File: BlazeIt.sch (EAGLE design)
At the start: 29 parts, among them IC1 L293D, IC2 L293D, Q1 200mA/40V, Q2 200mA/40V, Q3 200mA/40V, Q4 200mA/40V, U3 V_REG_317SINK

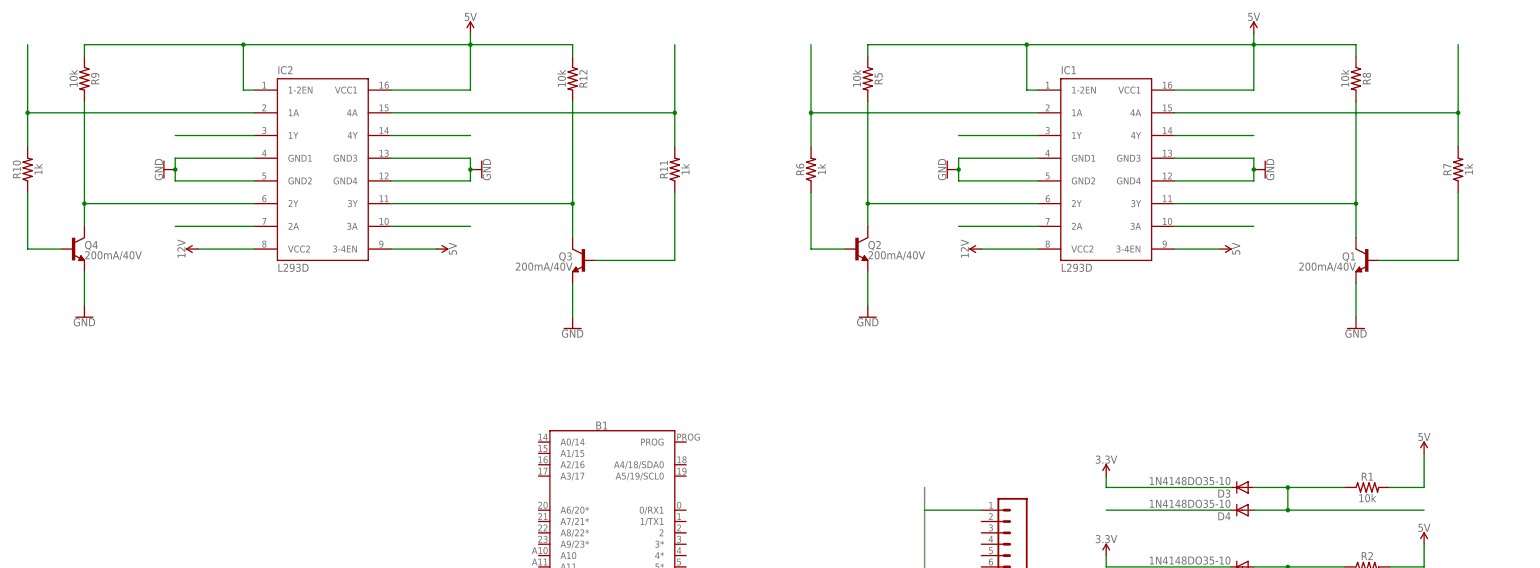
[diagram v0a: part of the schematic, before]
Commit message: added motor control wiring
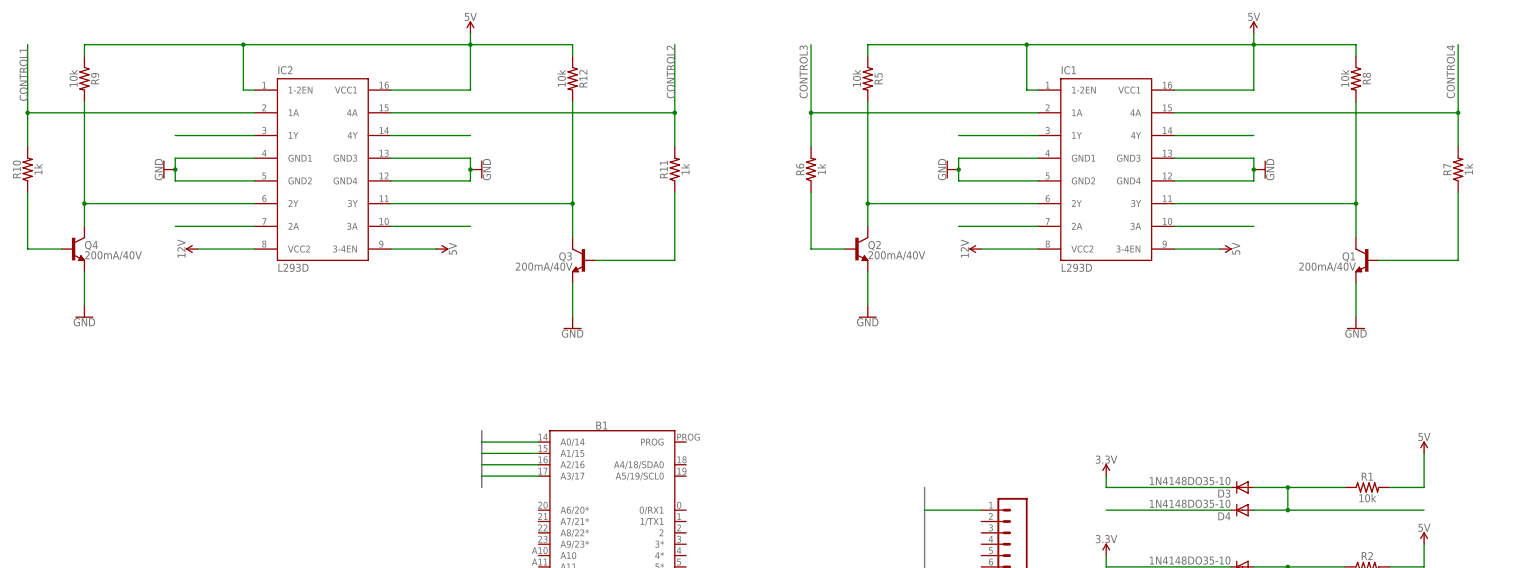
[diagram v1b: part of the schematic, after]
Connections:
- removed net N$13: IC1.1A, R6.2
- removed net N$21: IC1.4A, R7.2
- removed net N$24: IC2.1A, R10.2
- removed net N$31: IC2.4A, R11.2
- new net CONTROL1: B1.A0/14, IC2.1A, R10.2
- new net CONTROL2: B1.A1/15, IC2.4A, R11.2
- new net CONTROL3: B1.A2/16, IC1.1A, R6.2
- new net CONTROL4: B1.A3/17, IC1.4A, R7.2
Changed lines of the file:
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@@
+</segment>
+</bus>
+<bus name="CONTROL[1..4]">
+<segment>
+<wire x1="33.02" y1="86.36" x2="33.02" y2="73.66" width="0.762" layer="92"/>
 </segment>
 </bus>
@@
 </segment>
 </net>
-<net name="N$13" class="0">
+<net name="CONTROL3" class="0">
 <segment>
 <pinref part="R6" gate="G$1" pin="2"/>
@@
 <wire x1="157.48" y1="157.48" x2="106.68" y2="157.48" width="0.1524" layer="91"/>
 <junction x="106.68" y="157.48"/>
+<label x="104.14" y="172.72" size="1.778" layer="95" rot="R270"/>
+</segment>
+<segment>
+<pinref part="B1" gate="G$1" pin="A2/16"/>
+<wire x1="45.72" y1="78.74" x2="33.02" y2="78.74" width="0.1524" layer="91"/>
 </segment>
 </net>
@@
 </segment>
 </net>
-<net name="N$21" class="0">
+<net name="CONTROL4" class="0">
 <segment>
 <pinref part="R7" gate="G$1" pin="2"/>
@@
 <wire x1="187.96" y1="157.48" x2="251.46" y2="157.48" width="0.1524" layer="91"/>
 <junction x="251.46" y="157.48"/>
+<label x="248.92" y="172.72" size="1.778" layer="95" rot="R270"/>
+</segment>
+<segment>
+<pinref part="B1" gate="G$1" pin="A3/17"/>
+<wire x1="45.72" y1="76.2" x2="33.02" y2="76.2" width="0.1524" layer="91"/>
 </segment>
 </net>
@@
 </segment>
 </net>
-<net name="N$24" class="0">
+<net name="CONTROL1" class="0">
 <segment>
 <pinref part="R10" gate="G$1" pin="2"/>
@@
 <wire x1="-17.78" y1="157.48" x2="-68.58" y2="157.48" width="0.1524" layer="91"/>
 <junction x="-68.58" y="157.48"/>
+<label x="-68.58" y="160.02" size="1.778" layer="95" rot="R90"/>
+</segment>
+<segment>
+<pinref part="B1" gate="G$1" pin="A0/14"/>
+<wire x1="45.72" y1="83.82" x2="33.02" y2="83.82" width="0.1524" layer="91"/>
 </segment>
 </net>
@@
 </segment>
 </net>
-<net name="N$31" class="0">
+<net name="CONTROL2" class="0">
 <segment>
 <pinref part="R11" gate="G$1" pin="2"/>
@@
 <wire x1="12.7" y1="157.48" x2="76.2" y2="157.48" width="0.1524" layer="91"/>
 <junction x="76.2" y="157.48"/>
-</segment>
-</net>
+<label x="76.2" y="172.72" size="1.778" layer="95" rot="MR270"/>
+</segment>
+<segment>
+<pinref part="B1" gate="G$1" pin="A1/15"/>
+<wire x1="45.72" y1="81.28" x2="33.02" y2="81.28" width="0.1524" layer="91"/>
+</segment>
+</net>

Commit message: Added sensor pins
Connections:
- removed net SENSORS0: J1.1
- new net SENSOR1: B1.A6/20*, J1.1
- new net SENSOR2: B1.A7/21*, J1.2
- new net SENSOR3: B1.A8/22*, J1.3
- new net SENSOR4: B1.A9/23*, J1.4
- new net SENSOR5: B1.A10, J1.5
- new net SENSOR6: B1.A11, J1.6
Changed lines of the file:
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@@
 </instances>
 <busses>
-<bus name="SENSORS[0..7]">
-<segment>
-<wire x1="132.08" y1="73.66" x2="132.08" y2="35.56" width="0.762" layer="92"/>
+<bus name="CONTROL[1..4]">
+<segment>
+<wire x1="33.02" y1="86.36" x2="33.02" y2="73.66" width="0.762" layer="92"/>
+<label x="33.02" y="73.66" size="1.778" layer="95" rot="R90"/>
 </segment>
 </bus>
-<bus name="CONTROL[1..4]">
-<segment>
-<wire x1="33.02" y1="86.36" x2="33.02" y2="73.66" width="0.762" layer="92"/>
+<bus name="SENSOR[1..6]">
+<segment>
+<wire x1="129.54" y1="71.12" x2="129.54" y2="55.88" width="0.762" layer="92"/>
+<label x="129.54" y="55.88" size="1.778" layer="95" rot="R90"/>
+</segment>
+<segment>
+<wire x1="33.02" y1="71.12" x2="33.02" y2="55.88" width="0.762" layer="92"/>
+<label x="33.02" y="55.88" size="1.778" layer="95" rot="R90"/>
 </segment>
 </bus>
@@
 </segment>
 </net>
-<net name="SENSORS0" class="0">
+<net name="SENSOR1" class="0">
 <segment>
 <pinref part="J1" gate="G$1" pin="1"/>
-<wire x1="144.78" y1="68.58" x2="132.08" y2="68.58" width="0.1524" layer="91"/>
-</segment>
-</net>
+<wire x1="144.78" y1="68.58" x2="129.54" y2="68.58" width="0.1524" layer="91"/>
+</segment>
+<segment>
+<pinref part="B1" gate="G$1" pin="A6/20*"/>
+<wire x1="45.72" y1="68.58" x2="33.02" y2="68.58" width="0.1524" layer="91"/>
+</segment>
+</net>
+<net name="SENSOR2" class="0">
+<segment>
+<pinref part="J1" gate="G$1" pin="2"/>
+<wire x1="144.78" y1="66.04" x2="129.54" y2="66.04" width="0.1524" layer="91"/>
+</segment>
+<segment>
+<pinref part="B1" gate="G$1" pin="A7/21*"/>
+<wire x1="45.72" y1="66.04" x2="33.02" y2="66.04" width="0.1524" layer="91"/>
+</segment>
+</net>
+<net name="SENSOR3" class="0">
+<segment>
+<pinref part="J1" gate="G$1" pin="3"/>
+<wire x1="144.78" y1="63.5" x2="129.54" y2="63.5" width="0.1524" layer="91"/>
+</segment>
+<segment>
+<pinref part="B1" gate="G$1" pin="A8/22*"/>
+<wire x1="45.72" y1="63.5" x2="33.02" y2="63.5" width="0.1524" layer="91"/>
+</segment>
+</net>
+<net name="SENSOR4" class="0">
+<segment>
+<pinref part="J1" gate="G$1" pin="4"/>
+<wire x1="144.78" y1="60.96" x2="129.54" y2="60.96" width="0.1524" layer="91"/>
+</segment>
+<segment>
+<pinref part="B1" gate="G$1" pin="A9/23*"/>
+<wire x1="45.72" y1="60.96" x2="33.02" y2="60.96" width="0.1524" layer="91"/>
+</segment>
+</net>
+<net name="SENSOR5" class="0">
+<segment>
+<pinref part="J1" gate="G$1" pin="5"/>
+<wire x1="144.78" y1="58.42" x2="129.54" y2="58.42" width="0.1524" layer="91"/>
+</segment>
+<segment>
+<pinref part="B1" gate="G$1" pin="A10"/>
+<wire x1="45.72" y1="58.42" x2="33.02" y2="58.42" width="0.1524" layer="91"/>
+</segment>
+</net>
+<net name="SENSOR6" class="0">
+<segment>
+<pinref part="J1" gate="G$1" pin="6"/>
+<wire x1="144.78" y1="55.88" x2="129.54" y2="55.88" width="0.1524" layer="91"/>
+</segment>
+<segment>
+<pinref part="B1" gate="G$1" pin="A11"/>
+<wire x1="45.72" y1="55.88" x2="33.02" y2="55.88" width="0.1524" layer="91"/>
+</segment>
+</net>

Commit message: Added sensor pins to schematic
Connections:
- removed net N$1: D3.A, D4.A, R1.1
- removed net N$2: D1.A, D2.A, R2.1
- removed net N$3: D5.A, D6.A, R3.1
- removed net N$4: D7.A, D8.A, R4.1
- removed net N$5: D8.C
- removed net N$6: D6.C
- removed net N$7: D2.C
- removed net N$8: D4.C
- new net MOTOR1: D3.A, D4.A, IC2.1A, R1.1, R10.2
- new net MOTOR2: D1.A, D2.A, IC2.4A, R11.2, R2.1
- new net MOTOR3: D5.A, D6.A, IC1.1A, R3.1, R6.2
- new net MOTOR4: D7.A, D8.A, IC1.4A, R4.1, R7.2
- new net SWITCHES1: B1.2, J1.7
- new net SWITCHES2: B1.3*, J1.8
- new net SWITCHES3: B1.4*, J1.9
- new net SWITCHES4: B1.5*, J1.10
- net 5V: now also J1.11
- net CONTROL1: now also D4.C; no longer IC2.1A, R10.2
- net CONTROL2: now also D2.C; no longer IC2.4A, R11.2
- net CONTROL3: now also D6.C; no longer IC1.1A, R6.2
- net CONTROL4: now also D8.C; no longer IC1.4A, R7.2
- net GND: now also J1.12
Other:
- moved on the sheet: J1

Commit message: Finished Schematic Draft
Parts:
- added C1, C2: 0.1uF, SparkFun-Capacitors:0.1UF-KIT-EZ-50V-20%
- added FRAME1: FRAME-LEDGER, SparkFun-Aesthetics:FRAME-LEDGER
- added MOTOR1, MOTOR2: (no value), pinhead:PINHD-1X4
- added PAD1: 14V, wirepad:WIREPADSMD2,54-5,08
- added PAD2: GND PAD, wirepad:WIREPADSMD2,54-5,08
- added R13: 1k, SparkFun-Resistors:10KOHM-HORIZ-1/4W-1%
- added R14: 330, SparkFun-Resistors:10KOHM-HORIZ-1/4W-1%
- U3: value V_REG_317SINK -> LM317
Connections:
- removed net N$11: IC1.2Y, Q2.C, R5.2
- removed net N$14: IC1.1Y
- removed net N$18: IC1.3Y, Q1.C, R8.2
- removed net N$25: IC2.1Y
- removed net N$29: IC2.3Y, Q3.C, R12.2
- new net N$1: IC2.1Y, MOTOR1.3
- new net N$2: IC1.1Y, MOTOR2.3
- new net N$3: IC2.3Y, MOTOR1.1
- new net N$4: IC1.2Y, MOTOR2.4
- new net N$5: IC1.3Y, MOTOR2.1
- new net N$6: R13.1, R14.2, U3.ADJ
- net 12V: now also C1.1, PAD1.P, U3.IN
- net 3.3V: now also B1.3.3V
- net 5V: now also B1.VIN, C2.1, R14.1, U3.OUT
- net GND: now also B1.AGND, B1.GND, B1.GND1, C1.2, C2.2, PAD2.P, R13.2
- net N$15: now also Q2.C, R5.2
- net N$16: now also MOTOR2.2
- net N$17: now also Q1.C, R8.2
- net N$23: now also IC2.2A; no longer IC2.2Y
- net N$26: now also IC2.2Y, MOTOR1.4; no longer IC2.2A
- net N$27: now also MOTOR1.2
- net N$28: now also Q3.C, R12.2
- net SENSOR1: now also B1.2; no longer B1.A6/20*
- net SENSOR2: now also B1.3*; no longer B1.A7/21*
- net SENSOR3: now also B1.4*; no longer B1.A8/22*
- net SENSOR4: now also B1.5*; no longer B1.A9/23*
- net SENSOR5: now also B1.6*; no longer B1.A10
- net SENSOR6: now also B1.7/RX3; no longer B1.A11
- net SWITCHES1: now also B1.A6/20*; no longer B1.2
- net SWITCHES2: now also B1.A7/21*; no longer B1.3*
- net SWITCHES3: now also B1.A8/22*; no longer B1.4*
- net SWITCHES4: now also B1.A9/23*; no longer B1.5*
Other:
- moved on the sheet: B1, J1, U3

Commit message: Fixed some inconsistencies
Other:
- moved on the sheet: B1, C1, C2, D1, D2, D3, D4, D5, D6, D7, D8, IC1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

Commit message: Finalized Design
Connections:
- net 3.3V: now also B1.3V; no longer B1.3.3V
- net CONTROL1: now also B1.A3/17; no longer B1.A0/14
- net CONTROL2: now also B1.A2/16; no longer B1.A1/15
- net CONTROL3: now also B1.A1/15; no longer B1.A2/16
- net CONTROL4: now also B1.A0/14; no longer B1.A3/17
- net SENSOR1: now also B1.0/RX1; no longer B1.2
- net SENSOR2: now also B1.1/TX1; no longer B1.3*
- net SENSOR3: now also B1.2; no longer B1.4*
- net SENSOR4: now also B1.3*; no longer B1.5*
- net SENSOR5: now also B1.4*; no longer B1.6*
- net SENSOR6: now also B1.5*; no longer B1.7/RX3
- net SWITCHES1: now also B1.6*; no longer B1.A6/20*
- net SWITCHES2: now also B1.7/RX3; no longer B1.A7/21*
- net SWITCHES3: now also B1.8/TX3; no longer B1.A8/22*
- net SWITCHES4: now also B1.9*/RX2; no longer B1.A9/23*

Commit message: Final final design
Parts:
- removed R11: 1k, SparkFun-Resistors:1KOHM-HORIZ-1/4W-1%
- removed R12: 10k, SparkFun-Resistors:10KOHM-HORIZ-1/4W-1%
- removed R13: 1k, SparkFun-Resistors:10KOHM-HORIZ-1/4W-1%
- removed R14: 330, SparkFun-Resistors:10KOHM-HORIZ-1/4W-1%
- added D10, D11, D12, D13, D14, D15, D16, D17, D18, D19, D20, D21, D22, D23, D24, D9: DIODE-SCHOTTKY-PMEG4005EJ, SparkFun-DiscreteSemi:DIODE-SCHOTTKY-PMEG4005EJ
- added J2: (no value), SparkFun-Connectors:CONN_07LOCK
- C1, C2: device SparkFun-Capacitors:0.1UF-KIT-EZ-50V-20% -> SparkFun-Capacitors:0.1UF-0603-25V-5%
- D1, D2, D3, D4, D5, D6, D7, D8: value 1N4148DO35-10 -> DIODE-SCHOTTKY-PMEG4005EJ; device diode:1N4148DO35-10 -> SparkFun-DiscreteSemi:DIODE-SCHOTTKY-PMEG4005EJ
- Q1, Q2, Q3, Q4: value 200mA/40V -> MOSFET-NCH-2N7002PW; device SparkFun-DiscreteSemi:TRANS_NPN-2N3904 -> SparkFun-DiscreteSemi:MOSFET-NCH-2N7002PW
- R1, R2, R3, R4, R5, R8: device SparkFun-Resistors:10KOHM-HORIZ-1/4W-1% -> SparkFun-Resistors:10KOHM-0603-1/10W-1%
- R10: value 1k -> 330; device SparkFun-Resistors:1KOHM-HORIZ-1/4W-1% -> SparkFun-Resistors:3.3KOHM-0603-1/10W-1%
- R6, R7: value 1k -> 10k; device SparkFun-Resistors:1KOHM-HORIZ-1/4W-1% -> SparkFun-Resistors:10KOHM-0603-1/10W-1%
- R9: value 10k -> 1k; device SparkFun-Resistors:10KOHM-HORIZ-1/4W-1% -> SparkFun-Resistors:1KOHM-0603-1/10W-1%
- renumbered PAD1 to V+, PAD2 to GND
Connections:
- removed net N$10: Q2.B, R6.1
- removed net N$15: IC1.2A, Q2.C, R5.2
- removed net N$16: IC1.4Y, MOTOR2.2
- removed net N$17: IC1.3A, Q1.C, R8.2
- removed net N$2: IC1.1Y, MOTOR2.3
- removed net N$20: Q1.B, R7.1
- removed net N$22: Q4.B, R10.1
- removed net N$23: IC2.2A, Q4.C, R9.2
- removed net N$26: IC2.2Y, MOTOR1.4
- removed net N$27: IC2.4Y, MOTOR1.2
- removed net N$28: IC2.3A, Q3.C, R12.2
- removed net N$3: IC2.3Y, MOTOR1.1
- removed net N$30: Q3.B, R11.1
- removed net N$4: IC1.2Y, MOTOR2.4
- removed net N$5: IC1.3Y, MOTOR2.1
- new net EXPANSION1: B1.A6/20*, J2.1
- new net EXPANSION2: B1.A7/21*, J2.2
- new net EXPANSION3: B1.A8/22*, J2.3
- new net EXPANSION4: B1.A9/23*, J2.4
- new net EXPANSION5: B1.A4/18/SDA0, J2.5
- new net EXPANSION6: B1.A5/19/SCL0, J2.6
- new net EXPANSION7: B1.A14/DAC, J2.7
- new net INPUT1: IC2.2A, Q3.D, R5.1
- new net INPUT2: IC2.3A, Q4.D, R6.1
- new net INPUT3: IC1.2A, Q1.D, R7.1
- new net INPUT4: IC1.3A, Q2.D, R8.1
- new net PIN1: D10.A, D9.C, IC2.1Y, MOTOR1.4
- new net PIN2: D11.A, D12.C, IC2.2Y, MOTOR1.3
- new net PIN3: D13.C, D14.A, IC2.4Y, MOTOR1.2
- new net PIN4: D15.C, D16.A, IC2.3Y, MOTOR1.1
- new net PIN5: D17.C, D18.A, IC1.1Y, MOTOR2.4
- new net PIN6: D19.A, D20.C, IC1.2Y, MOTOR2.3
- new net PIN7: D21.C, D22.A, IC1.4Y, MOTOR2.2
- new net PIN8: D23.C, D24.A, IC1.3Y, MOTOR2.1
- net 12V: now also D10.C, D11.C, D14.C, D16.C, D18.C, D19.C, D22.C, D24.C
- net 5V: now also R10.2, R5.2, R6.2, R7.2, R8.2; no longer R12.1, R14.1, R5.1, R8.1, R9.1
- net CONTROL1: now also D2.C; no longer D4.C
- net CONTROL2: now also D4.C; no longer D2.C
- net GND: now also D12.A, D13.A, D15.A, D17.A, D20.A, D21.A, D23.A, D9.A, Q1.S, Q2.S, Q3.S, Q4.S, R9.1; no longer Q1.E, Q2.E, Q3.E, Q4.E, R13.2
- net MOTOR1: now also D1.A, D2.A, Q3.G; no longer D3.A, D4.A, R10.2
- net MOTOR2: now also D3.A, D4.A, Q4.G; no longer D1.A, D2.A, R11.2
- net MOTOR3: now also Q1.G; no longer R6.2
- net MOTOR4: now also Q2.G; no longer R7.2
- net N$1: now also B1.3.3V; no longer IC2.1Y, MOTOR1.3
- net N$6: now also R10.1, R9.2; no longer R13.1, R14.2
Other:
- moved on the sheet: IC1, MOTOR2, R10, R5, R6, R7, R8, R9
